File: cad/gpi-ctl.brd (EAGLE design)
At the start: 75 x 73.5 mm, 107 parts, among them CN1 HEADER-1X2.4, CN2 MICROSDPLAIN, CN3 1X4-BIG, J4 1X4-BIG, SW1 SWITCHGT12-THOLE, SW2 SWITCHKMR211, SW3 SWITCHKMR211, U1 STM32F4/64, U2 LMP8640, U3 ULN2003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

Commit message: tweak
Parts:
- C43: value (none) -> .1u
- R21: value (none) -> 100

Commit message: missing wire
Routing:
- net VCCA: track 139.7 -> 144.9 mm
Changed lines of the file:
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@@
 <grid distance="0.1" unitdist="mm" unit="mm" style="lines" multiple="10" display="yes" altdistance="0.025" altunitdist="inch" altunit="inch"/>
 <layers>
-<layer number="1" name="Top" color="4" fill="1" visible="no" active="yes"/>
+<layer number="1" name="Top" color="4" fill="1" visible="yes" active="yes"/>
 <layer number="2" name="power" color="5" fill="1" visible="no" active="yes"/>
 <layer number="3" name="Route3" color="4" fill="3" visible="no" active="no"/>
@@
 <layer number="15" name="signal" color="1" fill="1" visible="no" active="yes"/>
 <layer number="16" name="Bottom" color="6" fill="1" visible="no" active="yes"/>
-<layer number="17" name="Pads" color="2" fill="1" visible="no" active="yes"/>
-<layer number="18" name="Vias" color="2" fill="1" visible="no" active="yes"/>
+<layer number="17" name="Pads" color="2" fill="1" visible="yes" active="yes"/>
+<layer number="18" name="Vias" color="2" fill="1" visible="yes" active="yes"/>
 <layer number="19" name="Unrouted" color="6" fill="1" visible="yes" active="yes"/>
 <layer number="20" name="Dimension" color="15" fill="1" visible="yes" active="yes"/>
 <layer number="21" name="tPlace" color="7" fill="1" visible="yes" active="yes"/>
 <layer number="22" name="bPlace" color="7" fill="1" visible="yes" active="yes"/>
-<layer number="23" name="tOrigins" color="15" fill="1" visible="no" active="yes"/>
-<layer number="24" name="bOrigins" color="15" fill="1" visible="no" active="yes"/>
+<layer number="23" name="tOrigins" color="15" fill="1" visible="yes" active="yes"/>
+<layer number="24" name="bOrigins" color="15" fill="1" visible="yes" active="yes"/>
 <layer number="25" name="tNames" color="7" fill="1" visible="no" active="yes"/>
 <layer number="26" name="bNames" color="7" fill="1" visible="no" active="yes"/>
-<layer number="27" name="tValues" color="7" fill="1" visible="yes" active="yes"/>
-<layer number="28" name="bValues" color="7" fill="1" visible="yes" active="yes"/>
+<layer number="27" name="tValues" color="7" fill="1" visible="no" active="yes"/>
+<layer number="28" name="bValues" color="7" fill="1" visible="no" active="yes"/>
 <layer number="29" name="tStop" color="7" fill="3" visible="no" active="yes"/>
 <layer number="30" name="bStop" color="7" fill="6" visible="no" active="yes"/>
@@
 <wire x1="76.05" y1="21.35" x2="76.05" y2="21.8" width="0.35" layer="1"/>
 <wire x1="76.05" y1="21.8" x2="74" y2="21.8" width="0.35" layer="1"/>
+<wire x1="75.55" y1="12.1" x2="75.1" y2="12.1" width="0.35" layer="1"/>
+<wire x1="75.1" y1="12.1" x2="74.7" y2="11.7" width="0.35" layer="1"/>
+<wire x1="74.7" y1="11.7" x2="74.7" y2="7.5" width="0.35" layer="1"/>
 <wire x1="74" y1="17.1" x2="74" y2="21.8" width="0" layer="19" extent="1-15"/>
-<wire x1="75.55" y1="12.1" x2="75" y2="16.1" width="0" layer="19" extent="1-15"/>
 </signal>
 <signal name="N$29">

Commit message: bigger cap
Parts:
- C10, C17: value .001u -> .1u
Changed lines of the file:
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@@
 <attribute name="VALUE" x="33" y="55.284" size="1" layer="27" rot="R180"/>
 </element>
-<element name="C10" library="jaw" package="SMD0603" value=".001u" x="48.1" y="63.4" smashed="yes">
+<element name="C10" library="jaw" package="SMD0603" value=".1u" x="48.1" y="63.4" smashed="yes">
 <attribute name="NAME" x="51.022" y="63.016" size="1" layer="25" font="vector" ratio="10"/>
 <attribute name="VALUE" x="50.822" y="63.114" size="1" layer="27" font="vector" ratio="10"/>
@@
 <attribute name="VALUE" x="32.978" y="60.486" size="1" layer="27" font="vector" ratio="10" rot="R180"/>
 </element>
-<element name="C17" library="jaw" package="SMD0603" value=".001u" x="35.3" y="56.6" smashed="yes" rot="R180">
+<element name="C17" library="jaw" package="SMD0603" value=".1u" x="35.3" y="56.6" smashed="yes" rot="R180">
 <attribute name="NAME" x="37.422" y="56.116" size="1" layer="25" font="vector" ratio="10"/>
 <attribute name="VALUE" x="32.978" y="57.086" size="1" layer="27" font="vector" ratio="10" rot="R180"/>

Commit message: caps
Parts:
- C12: value .1u -> .01u
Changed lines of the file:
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@@
 <attribute name="VALUE" x="50.922" y="59.014" size="1" layer="27" font="vector" ratio="10"/>
 </element>
-<element name="C12" library="jaw" package="SMD0603" value=".1u" x="48.1" y="54.9" smashed="yes">
+<element name="C12" library="jaw" package="SMD0603" value=".01u" x="48.1" y="54.9" smashed="yes">
 <attribute name="NAME" x="51.022" y="54.516" size="1" layer="25" font="vector" ratio="10"/>
 <attribute name="VALUE" x="50.922" y="54.514" size="1" layer="27" font="vector" ratio="10"/>

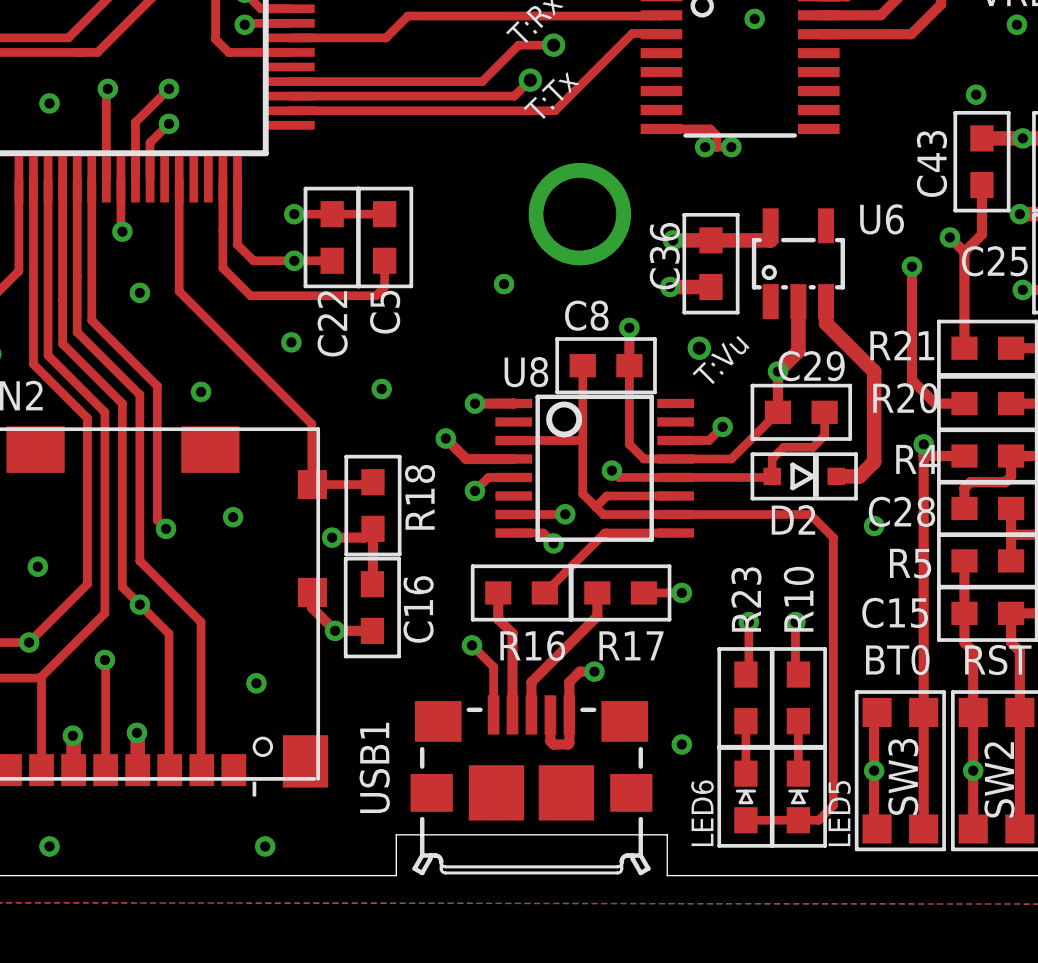
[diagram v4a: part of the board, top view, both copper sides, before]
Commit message: revert opamp, tweak
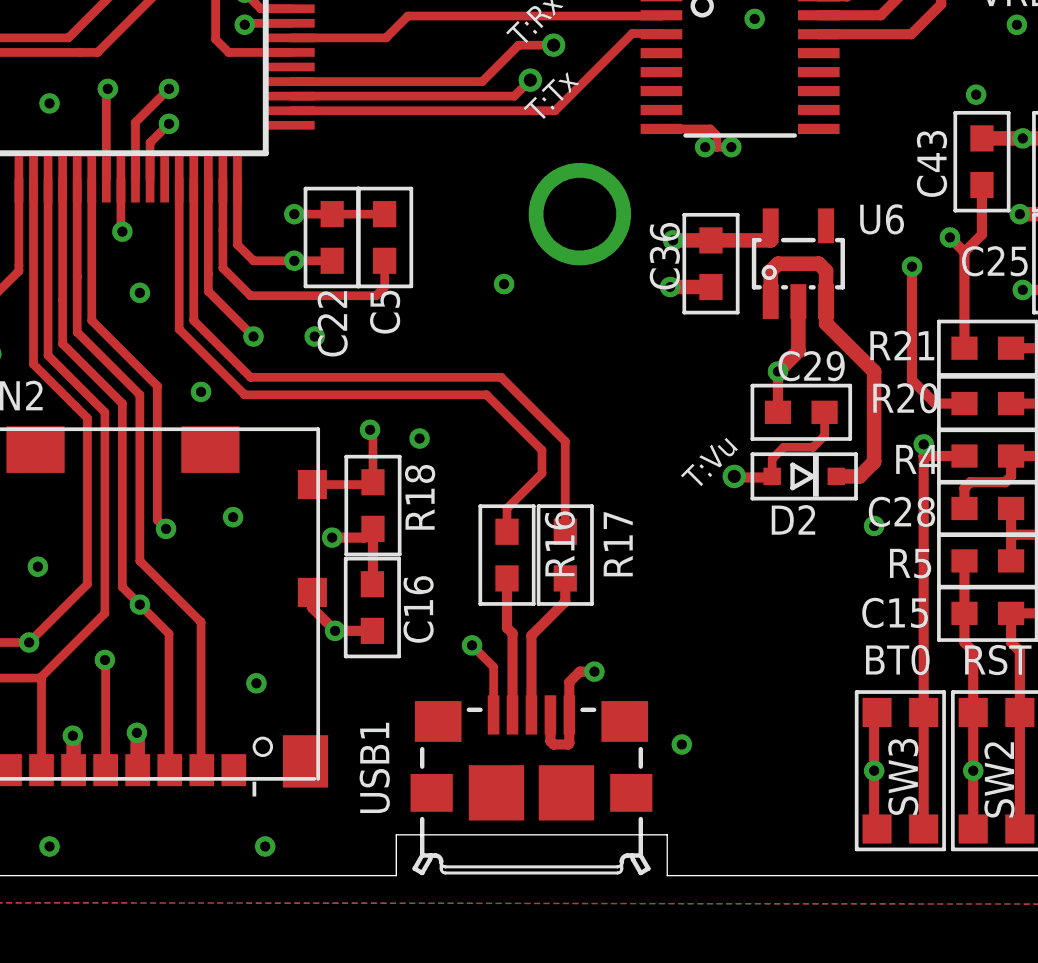
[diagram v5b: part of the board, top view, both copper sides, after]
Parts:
- removed C8: 2.2u, jaw:SMD0603
- removed LED5: GREEN, jaw:SMD0603D
- removed LED6: ORANGE, jaw:SMD0603D
- removed R10: 270, jaw:SMD0603
- removed R23: 560, jaw:SMD0603
- removed U8: IC_FT230X-SSOP-16, dp_devices:SSOP-16-FTDI
- moved R17 2.30 mm to (57.0, 11.0), turned to 270 degrees
- moved R16 1.39 mm to (55.0, 11.0), turned to 270 degrees
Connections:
- removed net N$20: R17.1, U8.8
- removed net N$25: R23.1, U8.7
- removed net N$26: R10.1, U8.14
- removed net N$38: LED5.C, R10.2
- removed net N$41: LED6.C, R23.2
- removed net N$42: R16.1, U8.9
- removed net USB3V3: C8.1, LED5.A, LED6.A, U8.10, U8.11, U8.3
- new net USBDM: R16.1, U1.44
- new net USBDP: R17.1, U1.45
- net GND: no longer C8.2, U8.13, U8.5
- net IOCARD: now also U1.46; no longer U1.44
- net RX: no longer U8.1
- net TX: no longer U8.4
- net VBUS: no longer U8.12
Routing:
- net USB3V3: track 31.3 -> 0.00 mm
- net USBDM: track 0.00 -> 22.6 mm
- net USBDP: track 0.00 -> 22.4 mm
- net TX: track 25.0 -> 8.43 mm, vias 2 -> 1
- net RX: track 24.9 -> 9.52 mm, vias 2 -> 1
- net N$25: track 13.0 -> 0.00 mm, vias 2 -> 0
- net GND: track 166.4 -> 154.9 mm, vias 118 -> 116
- net N$26: track 11.4 -> 0.00 mm, vias 2 -> 0
- net N$20: track 7.92 -> 0.00 mm, vias 2 -> 0
- net VBUS: track 26.0 -> 20.6 mm, vias 3 -> 2
- net N$42: track 5.34 -> 0.00 mm
- net N$8: track 7.69 -> 11.9 mm
- net N$41: track 1.80 -> 0.00 mm
- net N$38: track 1.80 -> 0.00 mm
- net IOCARD: track 14.5 -> 15.4 mm, vias 0 -> 2
